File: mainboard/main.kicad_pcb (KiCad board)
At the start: 2 copper layers, 36 parts, among them Q1 TIP120, U1 LevelShifter

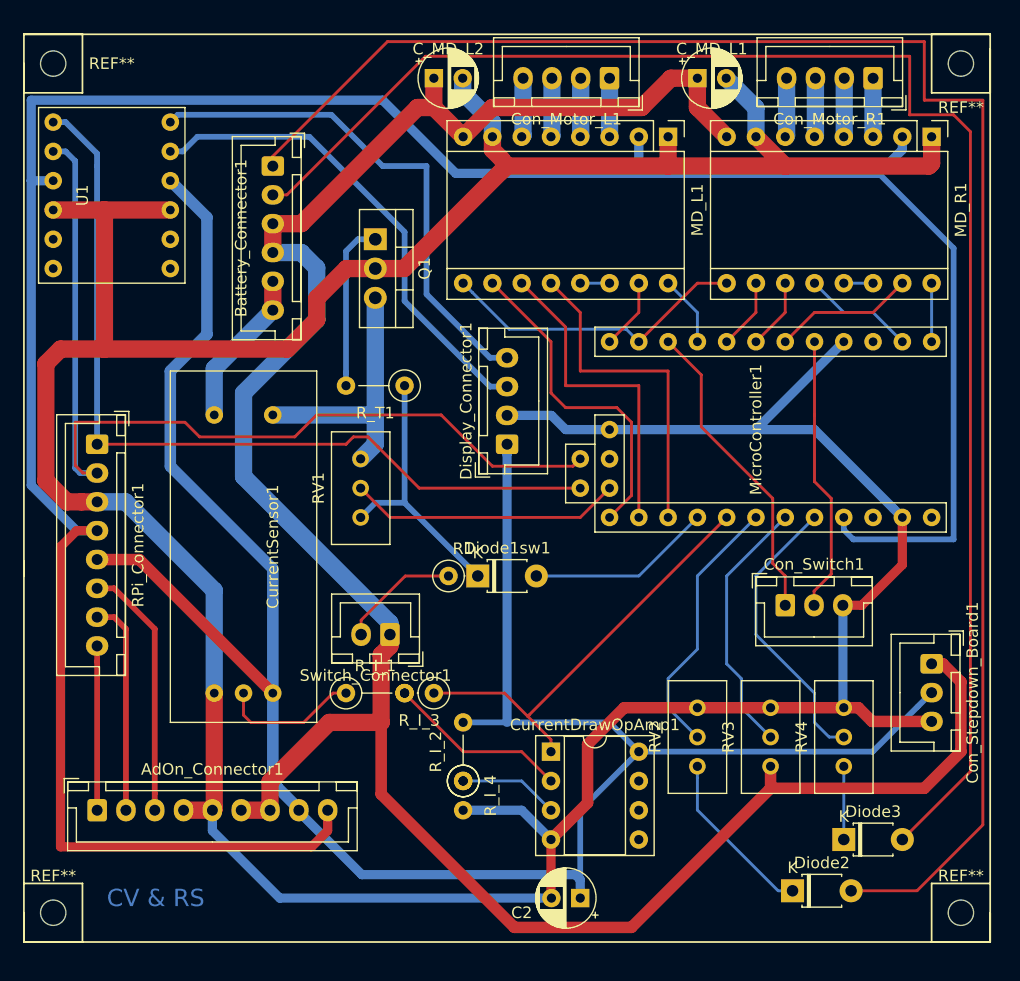
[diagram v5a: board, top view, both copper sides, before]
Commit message: Major re-layouting and cleanup
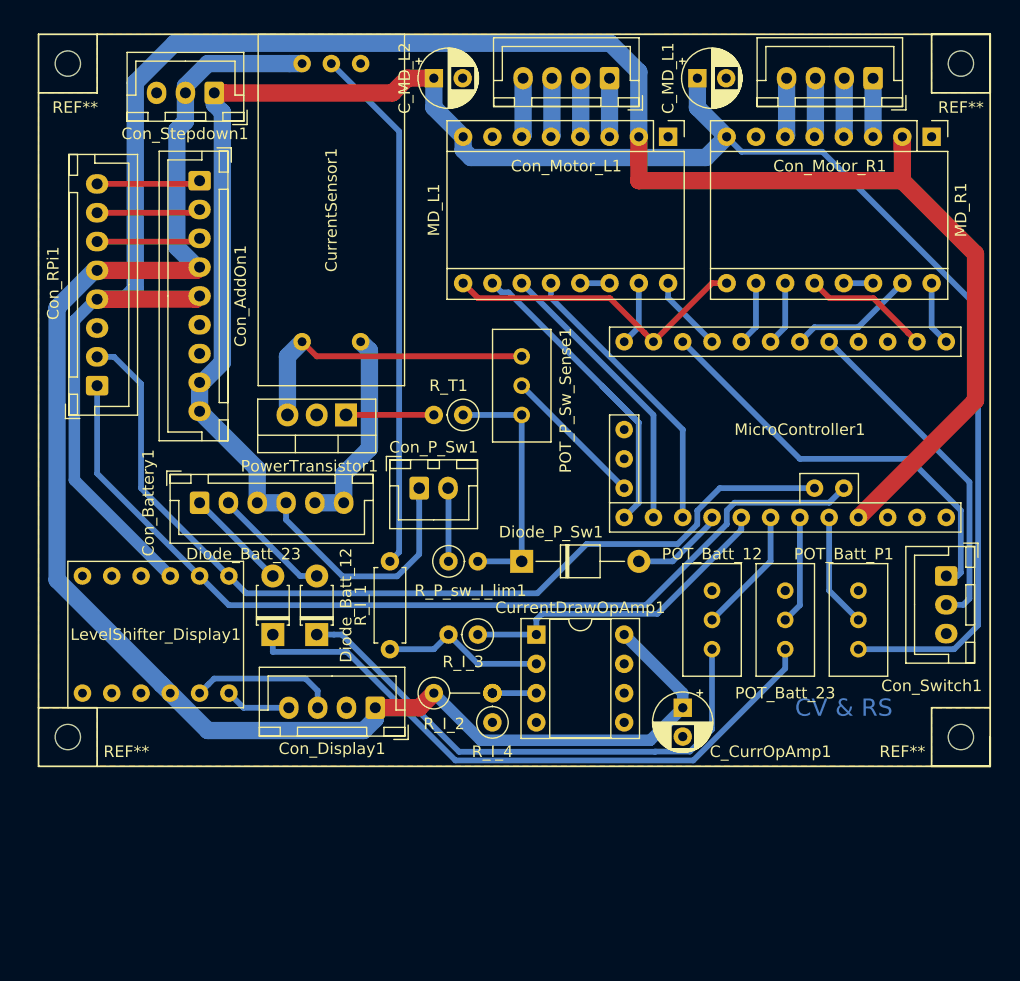
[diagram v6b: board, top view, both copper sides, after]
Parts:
- removed AdOn_Connector1: Conn_01x05, Connector_JST:JST_XH_B9B-XH-A_1x09_P2.50mm_Vertical
- removed Battery_Connector1: Conn_01x06, Connector_JST:JST_XH_B6B-XH-A_1x06_P2.50mm_Vertical
- removed C2: 1uF, Capacitor_THT:CP_Radial_D5.0mm_P2.50mm
- removed Diode1sw1, Diode2, Diode3: D, Diode_THT:D_T-1_P5.08mm_Horizontal
- removed Display_Connector1: Conn_01x04, Connector_JST:JST_XH_B4B-XH-A_1x04_P2.50mm_Vertical
- removed Q1: TIP120, Package_TO_SOT_THT:TO-220-3_Vertical
- removed R1: ?, Resistor_THT:R_Axial_DIN0207_L6.3mm_D2.5mm_P2.54mm_Vertical
- removed the REF** at (111.8, 102.9)
- removed the REF** at (190.5, 102.9)
- removed RV1: R_POT_TRIM, Potentiometer_THT:Potentiometer_Bourns_3296W_Vertical
- removed RV2: R_POT3Bat, Potentiometer_THT:Potentiometer_Bourns_3296W_Vertical
- removed RV3: R_POT2, Potentiometer_THT:Potentiometer_Bourns_3296W_Vertical
- removed RV4: R_POT1, Potentiometer_THT:Potentiometer_Bourns_3296W_Vertical
- removed Switch_Connector1: Conn_01x04, Connector_JST:JST_XH_B2B-XH-A_1x02_P2.50mm_Vertical
- removed U1: LevelShifter, CustomFootprints:LevelShifterBreakoutBoard
- added C_CurrOpAmp1: 1uF, Capacitor_THT:CP_Radial_D5.0mm_P2.50mm, F.Cu at (166.4, 85.1)
- added Con_AddOn1: Conn_01x05, Connector_JST:JST_XH_B9B-XH-A_1x09_P2.50mm_Vertical, F.Cu at (124.5, 39.4)
- added Con_Battery1: Conn_01x06, Connector_JST:JST_XH_B6B-XH-A_1x06_P2.50mm_Vertical, F.Cu at (124.5, 67.3)
- added Con_Display1: Conn_01x04, Connector_JST:JST_XH_B4B-XH-A_1x04_P2.50mm_Vertical, F.Cu at (139.7, 85.1)
- added Con_P_Sw1: Conn_01x04, Connector_JST:JST_XH_B2B-XH-A_1x02_P2.50mm_Vertical, F.Cu at (143.5, 66.0)
- added Diode_Batt_12: 1N 4448, Diode_THT:D_T-1_P5.08mm_Horizontal, F.Cu at (134.6, 78.7)
- added Diode_Batt_23: 1N 4448, Diode_THT:D_T-1_P5.08mm_Horizontal, F.Cu at (130.8, 78.7)
- added Diode_P_Sw1: 1N 4448, Diode_THT:D_T-1_P10.16mm_Horizontal, F.Cu at (152.4, 72.4)
- added LevelShifter_Display1: LevelShifter, CustomFootprints:LevelShifterBreakoutBoard, F.Cu at (119.4, 78.7)
- added POT_Batt_12: 1M, Potentiometer_THT:Potentiometer_Bourns_3296W_Vertical, F.Cu at (168.9, 74.9)
- added POT_Batt_23: 1M, Potentiometer_THT:Potentiometer_Bourns_3296W_Vertical, F.Cu at (175.3, 74.9)
- added POT_Batt_P1: 1M, Potentiometer_THT:Potentiometer_Bourns_3296W_Vertical, F.Cu at (181.6, 74.9)
- added POT_P_Sw_Sense1: 50k, Potentiometer_THT:Potentiometer_Bourns_3296W_Vertical, F.Cu at (152.4, 54.6)
- added PowerTransistor1: TIP120, Package_TO_SOT_THT:TO-220-3_Vertical, F.Cu at (137.2, 59.7)
- added REF**: MountingHole_2.2mm_M2, MountingHole:MountingHole_2.2mm_M2, F.Cu at (113.0, 87.6)
- added REF**: MountingHole_2.2mm_M2, MountingHole:MountingHole_2.2mm_M2, F.Cu at (190.5, 87.6)
- added R_P_sw_I_lim1: optional, Resistor_THT:R_Axial_DIN0207_L6.3mm_D2.5mm_P2.54mm_Vertical, F.Cu at (146.1, 72.4)
- MicroController1: footprint CustomFootprints:Arduino_Pro_Mini_Socket_IZOKEE_no_programming -> CustomFootprints:Arduino_Pro_Mini_Socket_IZOKEE_no_programming_no_ext_wire
- R_I_1: footprint Resistor_THT:R_Axial_DIN0207_L6.3mm_D2.5mm_P5.08mm_Vertical -> Resistor_THT:R_Axial_DIN0207_L6.3mm_D2.5mm_P7.62mm_Horizontal
- R_T1: footprint Resistor_THT:R_Axial_DIN0207_L6.3mm_D2.5mm_P5.08mm_Vertical -> Resistor_THT:R_Axial_DIN0207_L6.3mm_D2.5mm_P2.54mm_Vertical
- moved Con_Stepdown1 79.5 mm to (125.7, 31.8), turned to 180 degrees
- moved CurrentSensor1 30.2 mm to (135.9, 41.9), turned to 90 degrees
- moved Con_Switch1 14.2 mm to (189.2, 73.7), turned to 270 degrees
- moved R_I_1 12.0 mm to (141.0, 72.4), turned to 270 degrees
- moved CurrentDrawOpAmp1 10.2 mm to (153.7, 78.7)
- moved R_I_2 8.03 mm to (144.8, 83.8), turned to 0 degrees
- moved R_I_3 6.35 mm to (148.6, 78.7)
- moved R_I_4 5.68 mm to (149.9, 86.4), turned to 90 degrees
- moved R_T1 5.68 mm to (147.3, 59.7)
- moved Con_RPi1 5.08 mm to (115.6, 57.1), turned to 90 degrees
- moved MicroController1 1.27 mm to (176.5, 61.0)
- moved REF** 1.27 mm to (113.0, 29.2)
- renumbered RPi_Connector1 to Con_RPi1, Con_Stepdown_Board1 to Con_Stepdown1
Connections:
- net op1 renamed ADC_Batt_Curr
- Con_RPi1 pad 1: I2C_SDA -> I2C_SCL
- Con_RPi1 pad 2: I2C_SCL -> I2C_SDA
- CurrentSensor1 pad 4: Net-(Battery_Connector1-Pad5) -> -BATT
- MicroController1 pad 18: P_Check -> P_Sw_Sense
- MicroController1 pad 20: op2 -> ADC_Batt_12
- MicroController1 pad 21: op3 -> ADC_Batt_23
- MicroController1 pad 23: op4 -> ADC_Batt_P
- R_I_2 pad 1: Net-(CurrentDrawOpAmp1-Pad3) -> +5V
- R_I_2 pad 2: +5V -> Net-(CurrentDrawOpAmp1-Pad3)
- R_I_4 pad 1: Net-(CurrentDrawOpAmp1-Pad3) -> GND
- R_I_4 pad 2: GND -> Net-(CurrentDrawOpAmp1-Pad3)
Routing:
- net GND: track 369.0 -> 0.00 mm
- net BATT_Cell_2_3: track 148.3 -> 8.98 mm
- net BATT_Cell_1_2: track 135.0 -> 10.2 mm
- net Net-(Diode_Batt_23-Pad1): track 0.00 -> 54.8 mm
- net +5V: track 191.7 -> 138.3 mm
- net +3V3: track 226.7 -> 178.6 mm
- net Net-(Diode_Batt_12-Pad1): track 0.00 -> 46.3 mm
- net Net-(Display_Connector1-Pad4): track 44.7 -> 0.00 mm
- net Net-(Display_Connector1-Pad3): track 42.2 -> 0.00 mm
- net Net-(CurrentSensor1-Pad2): track 12.1 -> 45.9 mm
- net op4: track 25.1 -> 0.00 mm
- net P_Check: track 23.7 -> 0.00 mm
- net op2: track 23.3 -> 0.00 mm
- net op3: track 22.7 -> 0.00 mm
- net -BATT: track 0.00 -> 17.7 mm
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- added copper zone on F.Cu, net GND
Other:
- net class Default: clearance 0.2 -> 0.25; trace_width 0.25 -> 0.5
- net class HighPower added: clearance 0.25, trace_width 1.5, via_dia 0.8, via_drill 0.4
- net class LowPower added: clearance 0.25, trace_width 0.5, via_dia 0.8, via_drill 0.4
- net class Signal added: clearance 0.25, trace_width 0.5, via_dia 0.8, via_drill 0.4
- rule trace_clearance: 0.2 -> 0.25

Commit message: Minor polishing for submission
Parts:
- moved C_MD_L1 22.9 mm to (144.8, 30.5)
- moved C_MD_R1 22.9 mm to (167.6, 30.5)
- renumbered C_MD_L2 to C_MD_R1
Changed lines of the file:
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@@
   (general
     (thickness 1.6)
-    (drawings 18)
+    (drawings 21)
     (tracks 234)
     (zones 0)
@@
   (module CustomFootprints:Arduino_Pro_Mini_Socket_IZOKEE_no_programming_no_ext_wire (layer F.Cu)
     (at 176.53 60.96 270)
-    (fp_text reference MicroController1 (at 0 0) (layer F.SilkS)
+    (fp_text reference MicroController1 (at 0 -15.24 90) (layer F.SilkS)
       (effects (font (size 1 1) (thickness 0.15)))
     )
@@
       (effects (font (size 1 1) (thickness 0.15)))
     )
-    (fp_text value MountingHole_2.2mm_M2 (at 7.62 -5.715) (layer F.Fab)
+    (fp_text value MountingHole_2.2mm_M2 (at 3.81 -6.35) (layer F.Fab)
       (effects (font (size 1 1) (thickness 0.15)))
     )
@@
   )
   (module Capacitor_THT:CP_Radial_D5.0mm_P2.50mm (layer F.Cu)
-    (at 144.78 30.48)
+    (at 167.64 30.48)
     (descr "CP, Radial series, Radial, pin pitch=2.50mm, , diameter=5mm, Electrolytic Capacitor")
     (tags "CP Radial series Radial pin pitch 2.50mm  diameter 5mm Electrolytic Capacitor")
-    (fp_text reference C_MD_L2 (at -2.54 0 90) (layer F.SilkS)
+    (fp_text reference C_MD_R1 (at -2.54 0 90) (layer F.SilkS)
       (effects (font (size 1 1) (thickness 0.15)))
     )
@@
   )
   (module Capacitor_THT:CP_Radial_D5.0mm_P2.50mm (layer F.Cu)
-    (at 167.64 30.48)
+    (at 144.78 30.48)
     (descr "CP, Radial series, Radial, pin pitch=2.50mm, , diameter=5mm, Electrolytic Capacitor")
     (tags "CP Radial series Radial pin pitch 2.50mm  diameter 5mm Electrolytic Capacitor")
@@
     )
   )
-  (gr_text "CV & RS" (at 180.34 85.09) (layer B.Cu)
+  (dimension 2.54 (width 0.15) (layer F.Fab)
+    (gr_text "2.540 mm" (at 203.23 27.94 270) (layer F.Fab)
+      (effects (font (size 1 1) (thickness 0.15)))
+    )
+    (feature1 (pts (xy 193.04 29.21) (xy 202.516421 29.21)))
+    (feature2 (pts (xy 193.04 26.67) (xy 202.516421 26.67)))
+    (crossbar (pts (xy 201.93 26.67) (xy 201.93 29.21)))
+    (arrow1a (pts (xy 201.93 29.21) (xy 201.343579 28.083496)))
+    (arrow1b (pts (xy 201.93 29.21) (xy 202.516421 28.083496)))
+    (arrow2a (pts (xy 201.93 26.67) (xy 201.343579 27.796504)))
+    (arrow2b (pts (xy 201.93 26.67) (xy 202.516421 27.796504)))
+  )
+  (dimension 82.55 (width 0.15) (layer F.Fab)
+    (gr_text "82.550 mm" (at 151.765 19.02) (layer F.Fab)
+      (effects (font (size 1 1) (thickness 0.15)))
+    )
+    (feature1 (pts (xy 193.04 26.67) (xy 193.04 19.733579)))
+    (feature2 (pts (xy 110.49 26.67) (xy 110.49 19.733579)))
+    (crossbar (pts (xy 110.49 20.32) (xy 193.04 20.32)))
+    (arrow1a (pts (xy 193.04 20.32) (xy 191.913496 20.906421)))
+    (arrow1b (pts (xy 193.04 20.32) (xy 191.913496 19.733579)))
+    (arrow2a (pts (xy 110.49 20.32) (xy 111.616504 20.906421)))
+    (arrow2b (pts (xy 110.49 20.32) (xy 111.616504 19.733579)))
+  )
+  (dimension 63.5 (width 0.15) (layer F.Fab)
+    (gr_text "63.500 mm" (at 200.69 58.42 270) (layer F.Fab)
+      (effects (font (size 1 1) (thickness 0.15)))
+    )
+    (feature1 (pts (xy 193.04 90.17) (xy 199.976421 90.17)))
+    (feature2 (pts (xy 193.04 26.67) (xy 199.976421 26.67)))
+    (crossbar (pts (xy 199.39 26.67) (xy 199.39 90.17)))
+    (arrow1a (pts (xy 199.39 90.17) (xy 198.803579 89.043496)))
+    (arrow1b (pts (xy 199.39 90.17) (xy 199.976421 89.043496)))
+    (arrow2a (pts (xy 199.39 26.67) (xy 198.803579 27.796504)))
+    (arrow2b (pts (xy 199.39 26.67) (xy 199.976421 27.796504)))
+  )
+  (gr_text "CV & RS" (at 180.34 86.36) (layer B.Cu)
     (effects (font (size 1.5 1.5) (thickness 0.3)))
   )

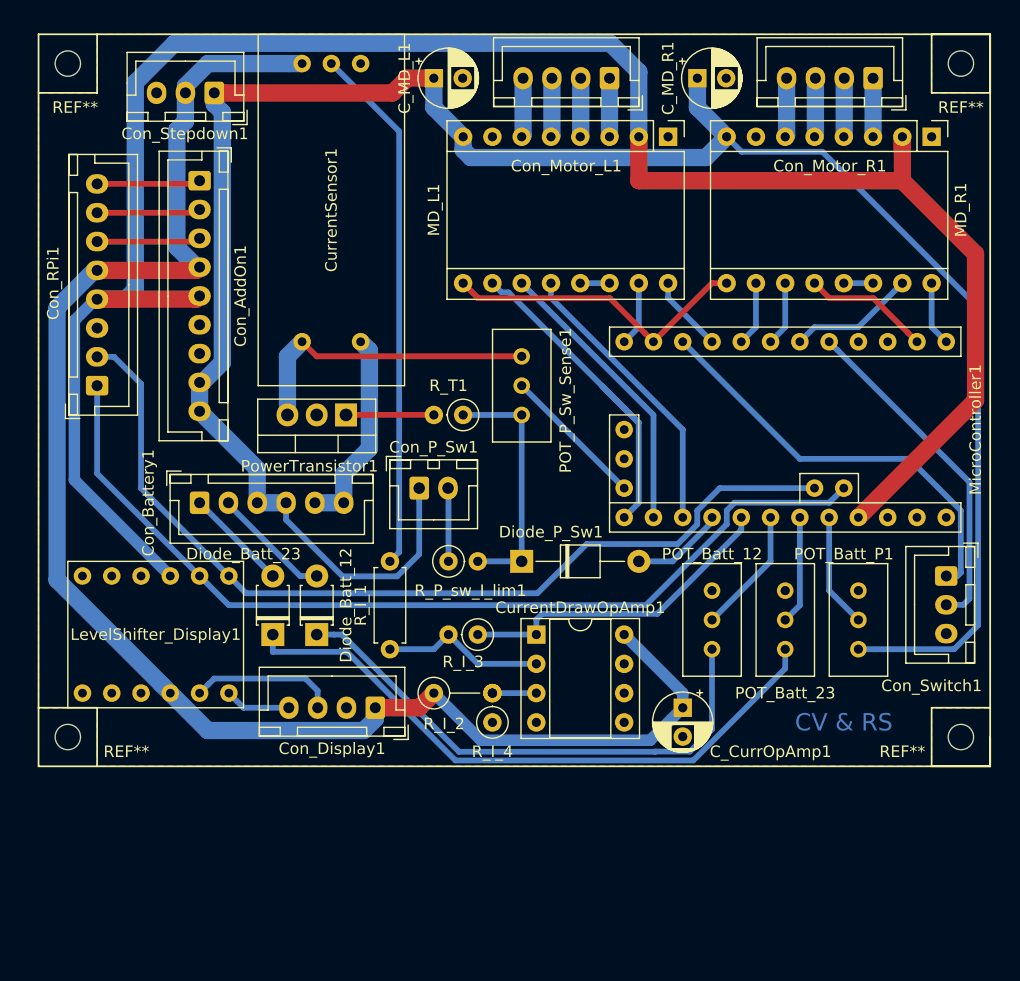
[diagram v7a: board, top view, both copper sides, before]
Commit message: mirrored CV&RS label, moved board outline to correct layer
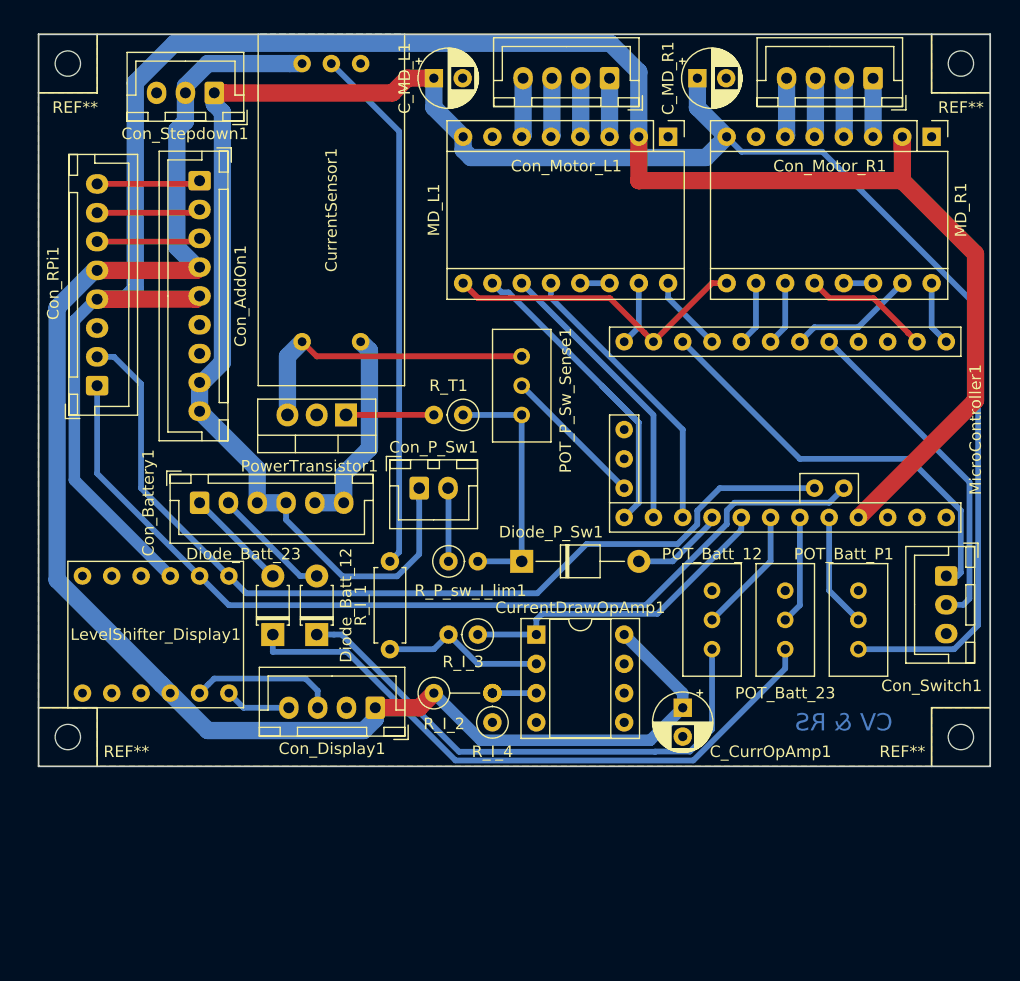
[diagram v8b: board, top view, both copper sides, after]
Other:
- board outline added: 82.5 x 63.5 mm
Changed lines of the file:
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@@
   (general
     (thickness 1.6)
-    (drawings 21)
+    (drawings 16)
     (tracks 234)
     (zones 0)
@@
     (47 F.CrtYd user)
     (48 B.Fab user)
-    (49 F.Fab user hide)
+    (49 F.Fab user)
   )
   (setup
@@
     (visible_elements 7FFFFFFF)
     (pcbplotparams
-      (layerselection 0x010fc_ffffffff)
+      (layerselection 0x010f0_ffffffff)
       (usegerberextensions false)
       (usegerberattributes false)
@@
       (outputformat 1)
       (mirror false)
-      (drillshape 1)
+      (drillshape 0)
       (scaleselection 1)
-      (outputdirectory ""))
+      (outputdirectory "Gerber/"))
   )
   (net 0 "")
@@
     )
   )
+  (gr_text "CV & RS" (at 180.34 86.36) (layer B.Cu)
+    (effects (font (size 1.5 1.5) (thickness 0.3)) (justify mirror))
+  )
   (dimension 2.54 (width 0.15) (layer F.Fab)
     (gr_text "2.540 mm" (at 203.23 27.94 270) (layer F.Fab)
@@
     (arrow2b (pts (xy 199.39 26.67) (xy 199.976421 27.796504)))
   )
-  (gr_text "CV & RS" (at 180.34 86.36) (layer B.Cu)
-    (effects (font (size 1.5 1.5) (thickness 0.3)))
-  )
-  (gr_line (start 193.04 26.67) (end 187.96 26.67) (layer F.SilkS) (width 0.15))
-  (gr_line (start 193.04 26.67) (end 193.04 31.75) (layer F.SilkS) (width 0.15))
   (gr_line (start 193.04 31.75) (end 187.96 31.75) (layer F.SilkS) (width 0.15))
   (gr_line (start 187.96 26.67) (end 187.96 31.75) (layer F.SilkS) (width 0.15))
@@
   (gr_line (start 115.57 85.09) (end 110.49 85.09) (layer F.SilkS) (width 0.15))
   (gr_line (start 115.57 85.09) (end 115.57 90.17) (layer F.SilkS) (width 0.15))
-  (gr_line (start 110.49 85.09) (end 110.49 90.17) (layer F.SilkS) (width 0.15))
   (gr_line (start 193.04 85.09) (end 187.96 85.09) (layer F.SilkS) (width 0.15))
-  (gr_line (start 193.04 87.63) (end 193.04 90.17) (layer F.SilkS) (width 0.15))
-  (gr_line (start 193.04 90.17) (end 187.96 90.17) (layer F.SilkS) (width 0.15))
   (gr_line (start 187.96 85.09) (end 187.96 90.17) (layer F.SilkS) (width 0.15))
-  (gr_line (start 110.49 26.67) (end 110.49 85.09) (layer F.SilkS) (width 0.15))
-  (gr_line (start 193.04 26.67) (end 193.04 90.17) (layer F.SilkS) (width 0.15))
-  (gr_line (start 110.49 26.67) (end 193.04 26.67) (layer F.SilkS) (width 0.15))
-  (gr_line (start 193.04 90.17) (end 110.49 90.17) (layer F.SilkS) (width 0.15))
+  (gr_line (start 110.49 26.67) (end 110.49 90.17) (layer Edge.Cuts) (width 0.15))
+  (gr_line (start 193.04 26.67) (end 193.04 90.17) (layer Edge.Cuts) (width 0.15))
+  (gr_line (start 110.49 26.67) (end 193.04 26.67) (layer Edge.Cuts) (width 0.15))
+  (gr_line (start 193.04 90.17) (end 110.49 90.17) (layer Edge.Cuts) (width 0.15))
   (segment (start 157.48 48.26) (end 160.02 48.26) (width 0.5) (layer B.Cu) (net 1))
   (segment (start 182.88 48.26) (end 180.34 48.26) (width 0.5) (layer B.Cu) (net 2))
